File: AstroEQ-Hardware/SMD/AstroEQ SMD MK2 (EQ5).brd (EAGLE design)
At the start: 85 x 49 mm, 41 parts, among them IC1 ATMEGA162-16AU, IC2 PIC18F14K50-I/SS, IC3 78L05, J1 POWER_JACKPANEL, M1 Motor Driver, M2 Motor Driver, SW1 SWITCH, X1 16MHz, X2 12MHz

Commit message: Correct Board-Schematic Inconsistencies
In the SMD design, the board and schematic files in Eagle had become
inconsistent. This has been corrected.
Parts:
- R15: device SmartPrj:R0603 -> rcl:R0603
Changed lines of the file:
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@@
 <?xml version="1.0" encoding="utf-8"?>
 <!DOCTYPE eagle SYSTEM "eagle.dtd">
-<eagle version="6.2">
+<eagle version="6.6.0">
 <drawing>
 <settings>
@@
 </class>
 </classes>
-<designrules>
+<designrules name="default">
 <description language="de">&lt;b&gt;EAGLE Design Rules&lt;/b&gt;
 &lt;p&gt;
@@
 <attribute name="MPN" value="GRM188R61C474KA93D" x="7.9375" y="24.13" size="1.778" layer="27" display="off"/>
 </element>
-<element name="R15" library="SmartPrj" package="R0603" value="1k" x="1.27" y="25.0825" smashed="yes" rot="R90">
+<element name="R15" library="rcl" package="R0603" value="1k" x="1.27" y="25.0825" smashed="yes" rot="R90">
 <attribute name="NAME" x="0.73025" y="23.4315" size="1.016" layer="25" font="vector" ratio="15" rot="R270"/>
 <attribute name="OC_FARNELL" value="2059601" x="1.27" y="25.0825" size="1.778" layer="27" rot="R90" display="off"/>

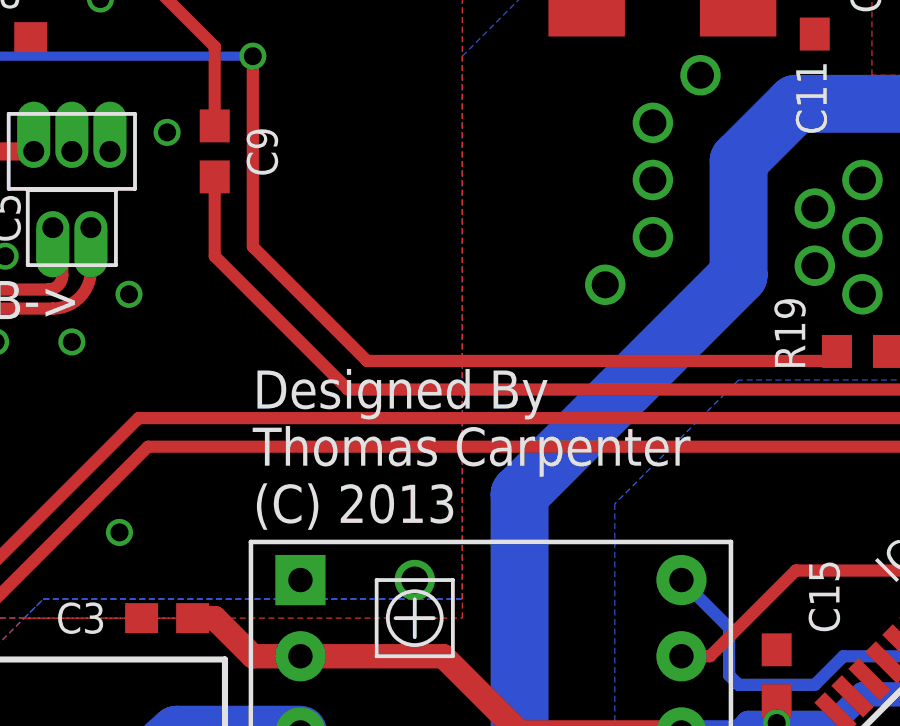
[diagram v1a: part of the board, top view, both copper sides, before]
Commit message: Update PCB Logo
Add AstroEQ logo to PCB hardware designs.
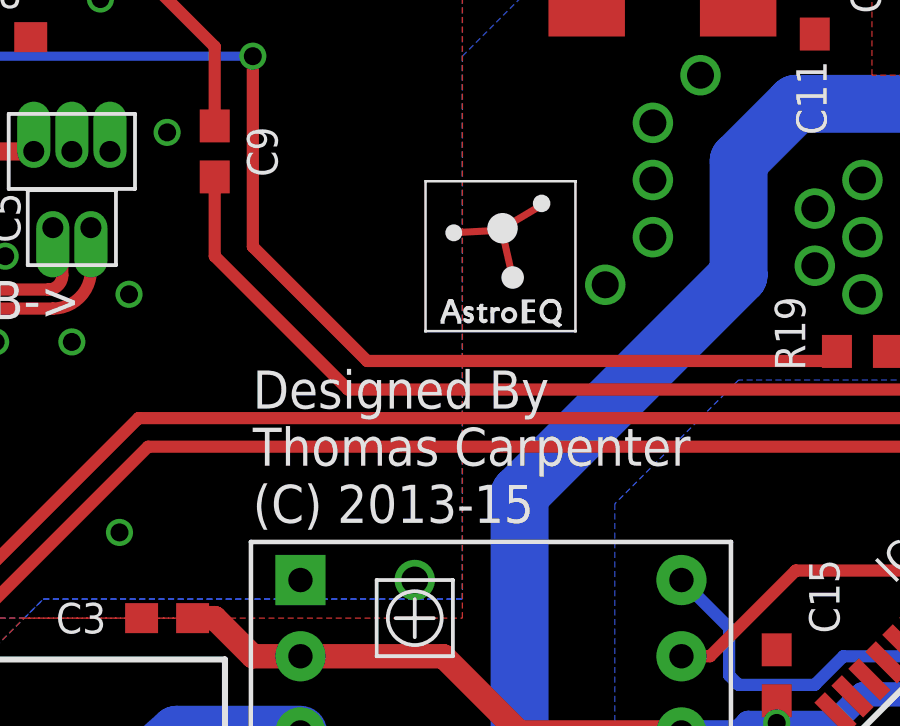
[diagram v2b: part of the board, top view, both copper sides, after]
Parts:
- added LOGO1: ASTROEQ5MM, AstroEQTooth:ASTROEQ-SMALL
- R15: device rcl:R0603 -> SmartPrj:R0603
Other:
- board text added: "(C) 2013-15"
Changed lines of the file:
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@@
 <layer number="43" name="vRestrict" color="2" fill="10" visible="no" active="yes"/>
 <layer number="44" name="Drills" color="15" fill="1" visible="no" active="yes"/>
-<layer number="45" name="Holes" color="15" fill="1" visible="no" active="yes"/>
+<layer number="45" name="Holes" color="15" fill="1" visible="yes" active="yes"/>
 <layer number="46" name="Milling" color="3" fill="1" visible="no" active="yes"/>
 <layer number="47" name="Measures" color="7" fill="1" visible="no" active="yes"/>
-<layer number="48" name="Document" color="7" fill="1" visible="no" active="yes"/>
+<layer number="48" name="Document" color="7" fill="1" visible="yes" active="yes"/>
 <layer number="49" name="Reference" color="7" fill="1" visible="yes" active="yes"/>
 <layer number="50" name="dxf" color="7" fill="1" visible="no" active="no"/>
-<layer number="51" name="tDocu" color="7" fill="1" visible="no" active="yes"/>
+<layer number="51" name="tDocu" color="7" fill="1" visible="yes" active="yes"/>
 <layer number="52" name="bDocu" color="7" fill="1" visible="no" active="yes"/>
 <layer number="53" name="tGND_GNDA" color="7" fill="9" visible="no" active="no"/>
@@
 <layer number="110" name="fp0" color="7" fill="1" visible="no" active="yes"/>
 <layer number="111" name="LPC17xx" color="7" fill="1" visible="no" active="yes"/>
+<layer number="112" name="tSilk" color="7" fill="1" visible="no" active="yes"/>
 <layer number="116" name="Patch_BOT" color="9" fill="4" visible="no" active="yes"/>
 <layer number="121" name="_tsilk" color="7" fill="1" visible="no" active="yes"/>
@@
 <layer number="124" name="bTestmark" color="7" fill="1" visible="no" active="yes"/>
 <layer number="125" name="_tNames" color="7" fill="1" visible="no" active="yes"/>
+<layer number="126" name="_bNames" color="7" fill="1" visible="no" active="yes"/>
+<layer number="127" name="_tValues" color="7" fill="1" visible="no" active="yes"/>
+<layer number="128" name="_bValues" color="7" fill="1" visible="no" active="yes"/>
 <layer number="131" name="tAdjust" color="7" fill="1" visible="no" active="yes"/>
 <layer number="132" name="bAdjust" color="7" fill="1" visible="no" active="yes"/>
 <layer number="144" name="Drill_legend" color="7" fill="1" visible="no" active="yes"/>
 <layer number="151" name="HeatSink" color="7" fill="1" visible="no" active="yes"/>
+<layer number="152" name="_bDocu" color="7" fill="1" visible="no" active="yes"/>
 <layer number="199" name="Contour" color="7" fill="1" visible="no" active="yes"/>
 <layer number="200" name="200bmp" color="1" fill="10" visible="no" active="yes"/>
@@
 <layer number="223" name="223bmp" color="24" fill="1" visible="no" active="no"/>
 <layer number="224" name="224bmp" color="25" fill="1" visible="no" active="no"/>
+<layer number="248" name="Housing" color="7" fill="1" visible="no" active="yes"/>
+<layer number="249" name="Edge" color="7" fill="1" visible="no" active="yes"/>
 <layer number="250" name="Descript" color="3" fill="1" visible="no" active="no"/>
 <layer number="251" name="SMDround" color="12" fill="11" visible="no" active="no"/>
@@
 <text x="23.1775" y="26.67" size="1.27" layer="25" font="vector" ratio="20">Designed By</text>
 <text x="23.1775" y="24.765" size="1.27" layer="25" font="vector" ratio="20">Thomas Carpenter</text>
-<text x="23.1775" y="22.86" size="1.27" layer="25" font="vector" ratio="20">(C) 2013</text>
+<text x="23.1775" y="22.86" size="1.27" layer="25" font="vector" ratio="20">(C) 2013-15</text>
 <wire x1="0" y1="0" x2="0" y2="49" width="0" layer="20"/>
 <wire x1="0" y1="49" x2="85" y2="49" width="0" layer="20"/>
@@
 <text x="2.54" y="53.34" size="1.778" layer="49">I use iteadstudio.com 10cm x 5cm prototype service, selecting 1.2mm thick, HASL, 100% electrical check</text>
 <text x="2.54" y="58.42" size="1.778" layer="49">The board uses some very tricky surface mount components and is not recommended for DIY.</text>
+<circle x="17.145" y="33.9725" radius="9.5" width="0.3048" layer="51"/>
+<wire x1="6.35" y1="18.415" x2="6.35" y2="4.445" width="0.4064" layer="51"/>
+<wire x1="17.78" y1="18.415" x2="17.78" y2="4.445" width="0.4064" layer="51"/>
+<wire x1="6.35" y1="18.415" x2="17.78" y2="18.415" width="0.4064" layer="51"/>
+<wire x1="6.35" y1="4.445" x2="17.78" y2="4.445" width="0.4064" layer="51"/>
+<circle x="73.9775" y="38.735" radius="5.75016875" width="0.4064" layer="51"/>
 </plain>
 <attributes>
@@
 <attribute name="MPN" value="GRM188R61C474KA93D" x="7.9375" y="24.13" size="1.778" layer="27" display="off"/>
 </element>
-<element name="R15" library="rcl" package="R0603" value="1k" x="1.27" y="25.0825" smashed="yes" rot="R90">
+<element name="R15" library="SmartPrj" package="R0603" value="1k" x="1.27" y="25.0825" smashed="yes" rot="R90">
 <attribute name="NAME" x="0.73025" y="23.4315" size="1.016" layer="25" font="vector" ratio="15" rot="R270"/>
 <attribute name="OC_FARNELL" value="2059601" x="1.27" y="25.0825" size="1.778" layer="27" rot="R90" display="off"/>
@@
 <attribute name="MPN" value="AE101J1V3B004" x="54.2925" y="41.275" size="1.778" layer="27" display="off"/>
 </element>
+<element name="LOGO1" library="AstroEQTooth" package="ASTROEQ-SMALL" value="ASTROEQ5MM" x="28.8925" y="29.21"/>
 </elements>
 <signals>
